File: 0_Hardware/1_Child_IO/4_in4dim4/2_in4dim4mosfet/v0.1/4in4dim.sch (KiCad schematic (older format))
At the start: 78 parts, among them IC1 TLP290, J1 RJ45, J2 RJ45, P1 CONN_5, P110 CONN_2, P120 CONN_2, P130 CONN_2, P140 CONN_2, P2 CONN_2, P3 CONN_8X2, Q1 SPP20N60C3, Q2 SPP20N60C3, Q3 SPP20N60C3, Q4 SPP20N60C3, U2 LTV847, U3 LTV847

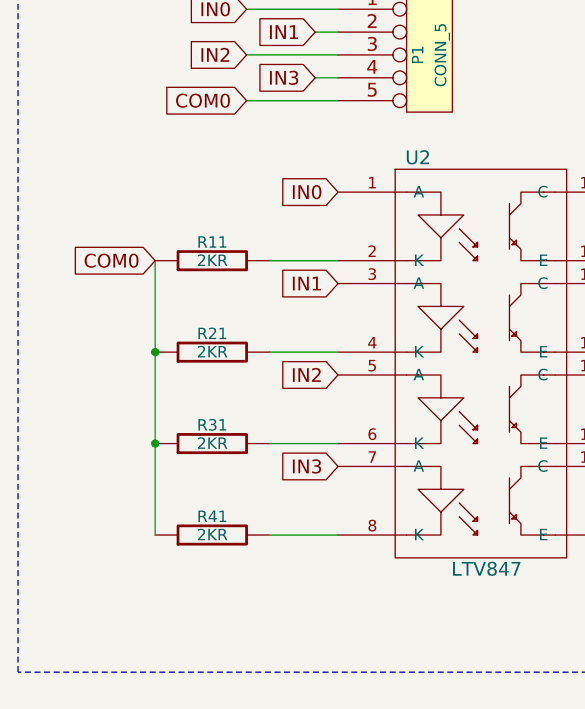
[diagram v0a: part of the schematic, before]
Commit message: mis à jour de la carte de puissance et de la front panel
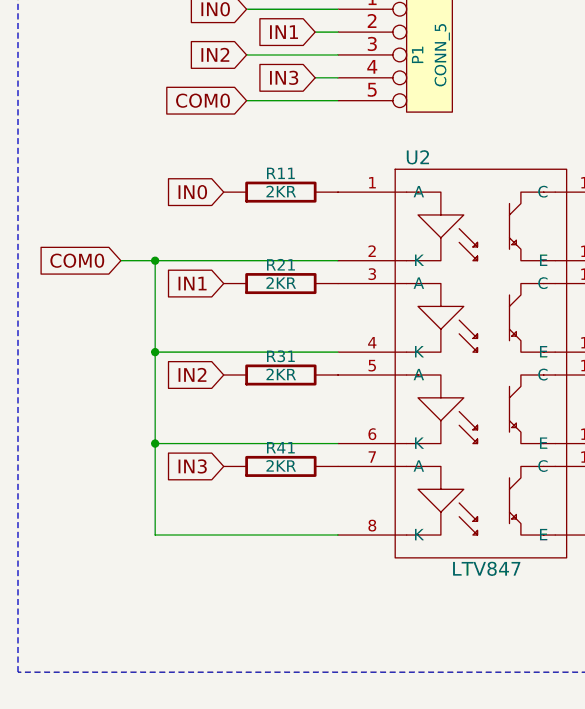
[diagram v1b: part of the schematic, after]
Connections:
- net COM0: now also U2.2 (K), U2.4 (K), U2.6 (K), U2.8 (K); no longer R11.1, R21.1, R31.1, R41.1
- net IN0: now also R11.1; no longer U2.1 (A)
- net IN1: now also R21.1; no longer U2.3 (A)
- net IN2: now also R31.1; no longer U2.5 (A)
- net IN3: now also R41.1; no longer U2.7 (A)
- net at R11.2: now also U2.1 (A); no longer U2.2 (K)
- net at R21.2: now also U2.3 (A); no longer U2.4 (K)
- net at R31.2: now also U2.5 (A); no longer U2.6 (K)
- net at R41.2: now also U2.7 (A); no longer U2.8 (K)
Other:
- moved on the sheet: R11, R21, R31, R41
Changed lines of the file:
@@
 LIBS:max485
 LIBS:4in4dim-cache
-EELAYER 24 0
+EELAYER 27 0
 EELAYER END
 $Descr A2 23386 16535
@@
 Sheet 1 1
 Title "4in 4dim power mosfet board"
-Date "10 mars 2014"
+Date "16 nov 2014"
 Rev "V0.0"
 Comp "XPLDUINO project"
@@
 L R R11
 U 1 1 51150759
-P 1900 2850
-F 0 "R11" V 1980 2850 50  0000 C CNN
-F 1 "2KR" V 1900 2850 50  0000 C CNN
-F 2 "" H 1900 2850 60  0001 C CNN
-F 3 "" H 1900 2850 60  0001 C CNN
-	1    1900 2850
+P 2200 2550
+F 0 "R11" V 2280 2550 50  0000 C CNN
+F 1 "2KR" V 2200 2550 50  0000 C CNN
+F 2 "" H 2200 2550 60  0001 C CNN
+F 3 "" H 2200 2550 60  0001 C CNN
+	1    2200 2550
 	0    -1   -1   0
 $EndComp
@@
 L R R21
 U 1 1 51150EEF
-P 1900 3250
-F 0 "R21" V 1980 3250 50  0000 C CNN
-F 1 "2KR" V 1900 3250 50  0000 C CNN
-F 2 "" H 1900 3250 60  0001 C CNN
-F 3 "" H 1900 3250 60  0001 C CNN
-	1    1900 3250
+P 2200 2950
+F 0 "R21" V 2280 2950 50  0000 C CNN
+F 1 "2KR" V 2200 2950 50  0000 C CNN
+F 2 "" H 2200 2950 60  0001 C CNN
+F 3 "" H 2200 2950 60  0001 C CNN
+	1    2200 2950
 	0    -1   -1   0
 $EndComp
@@
 L R R31
 U 1 1 51151110
-P 1900 3650
-F 0 "R31" V 1980 3650 50  0000 C CNN
-F 1 "2KR" V 1900 3650 50  0000 C CNN
-F 2 "" H 1900 3650 60  0001 C CNN
-F 3 "" H 1900 3650 60  0001 C CNN
-	1    1900 3650
+P 2200 3350
+F 0 "R31" V 2280 3350 50  0000 C CNN
+F 1 "2KR" V 2200 3350 50  0000 C CNN
+F 2 "" H 2200 3350 60  0001 C CNN
+F 3 "" H 2200 3350 60  0001 C CNN
+	1    2200 3350
 	0    -1   -1   0
 $EndComp
@@
 L R R41
 U 1 1 51151157
-P 1900 4050
-F 0 "R41" V 1980 4050 50  0000 C CNN
-F 1 "2KR" V 1900 4050 50  0000 C CNN
-F 2 "" H 1900 4050 60  0001 C CNN
-F 3 "" H 1900 4050 60  0001 C CNN
-	1    1900 4050
+P 2200 3750
+F 0 "R41" V 2280 3750 50  0000 C CNN
+F 1 "2KR" V 2200 3750 50  0000 C CNN
+F 2 "" H 2200 3750 60  0001 C CNN
+F 3 "" H 2200 3750 60  0001 C CNN
+	1    2200 3750
 	0    -1   -1   0
 $EndComp
@@
 Text GLabel 7450 7150 3    60   Input ~ 0
 /INT
-Text GLabel 2450 2550 0    60   Input ~ 0
+Text GLabel 1950 2550 0    60   Input ~ 0
 IN0
-Text GLabel 2450 2950 0    60   Input ~ 0
+Text GLabel 1950 2950 0    60   Input ~ 0
 IN1
-Text GLabel 2450 3350 0    60   Input ~ 0
+Text GLabel 1950 3350 0    60   Input ~ 0
 IN2
-Text GLabel 2450 3750 0    60   Input ~ 0
+Text GLabel 1950 3750 0    60   Input ~ 0
 IN3
 Text GLabel 8500 13700 2    60   BiDi ~ 0
@@
 Text GLabel 8200 13800 2    60   BiDi ~ 0
 SCL
-Text GLabel 1650 2850 0    60   Input ~ 0
+Text GLabel 1500 2850 0    60   Input ~ 0
 COM0
 $Comp
@@
 	9650 12600 5350 12600
 Wire Wire Line
-	2150 4050 2450 4050
-Wire Wire Line
-	2150 3650 2450 3650
-Wire Wire Line
-	2150 3250 2450 3250
-Wire Wire Line
-	2150 2850 2450 2850
+	1650 4050 2450 4050
+Wire Wire Line
+	1650 3650 2450 3650
+Wire Wire Line
+	1650 3250 2450 3250
+Wire Wire Line
+	1500 2850 2450 2850
 Wire Wire Line
 	1650 2850 1650 4050
@@
 	8050 13600 8250 13600
 NoConn ~ 7250 13600
+Connection ~ 1650 2850
 $EndSCHEMATC

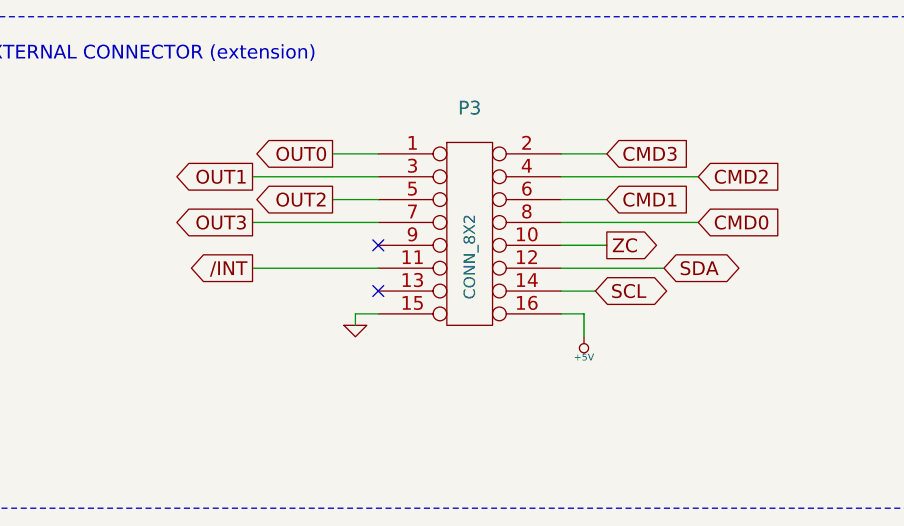
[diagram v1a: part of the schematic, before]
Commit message: Carte de puissance dimmer - modification du connecteur 20 broches: doublement de 5V et GND et optimisation pinout - modification empreinte des optos 4 canaux et single (création boitier DDIP16 et DDIP4) suite controle des packages des composants - routage pour tenir compte des changements de packages
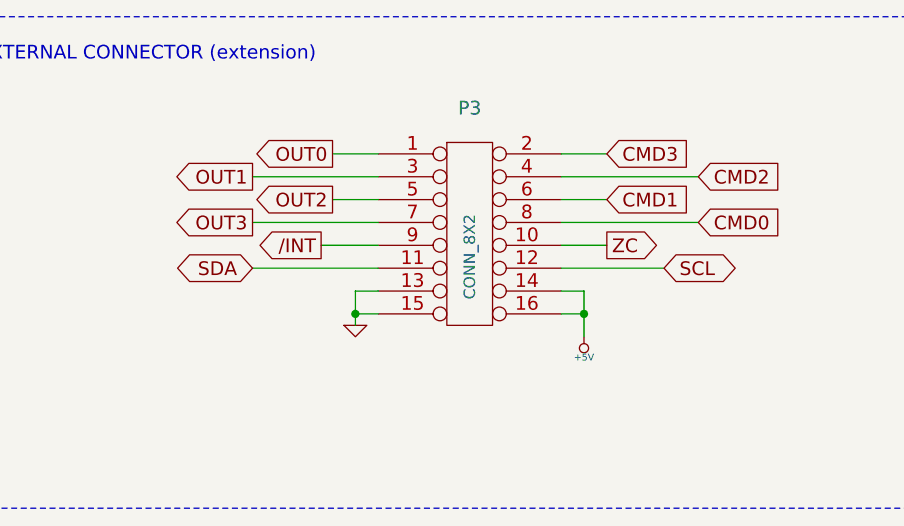
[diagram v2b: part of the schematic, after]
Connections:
- net +5V: now also P3.14
- net /INT: now also P3.9; no longer P3.11
- net GND: now also P3.13
- net SCL: now also P3.12; no longer P3.14
- net SDA: now also P3.11; no longer P3.12
- no-connect marks 2 -> 0
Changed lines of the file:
@@
 Sheet 1 1
 Title "4in 4dim power mosfet board"
-Date "16 nov 2014"
+Date "19 nov 2014"
 Rev "V0.0"
 Comp "XPLDUINO project"
@@
 Text GLabel 6150 7150 3    60   BiDi ~ 0
 SCL
-Text GLabel 6700 13700 0    60   Output ~ 0
+Text GLabel 7000 13600 0    60   Output ~ 0
 /INT
 Text GLabel 6350 7150 3    60   Input ~ 0
@@
 Text GLabel 1950 3750 0    60   Input ~ 0
 IN3
+Text GLabel 6700 13700 0    60   BiDi ~ 0
+SDA
 Text GLabel 8500 13700 2    60   BiDi ~ 0
-SDA
-Text GLabel 8200 13800 2    60   BiDi ~ 0
 SCL
 Text GLabel 1500 2850 0    60   Input ~ 0
@@
 	1    0    0    -1
 $EndComp
+Text Label 15350 5050 0    60   ~ 0
+110D
+Text Label 16550 7200 0    60   ~ 0
+110S
+Text Label 16650 12300 0    60   ~ 0
+120S
+Text Label 15400 10150 0    60   ~ 0
+120D
+Text Label 20200 5050 0    60   ~ 0
+130D
+Text Label 20250 10150 0    60   ~ 0
+140D
+Text Label 21400 7200 0    60   ~ 0
+130S
+Text Label 21450 12300 0    60   ~ 0
+140S
+$Comp
+L R RP1
+U 1 1 53162006
+P 18850 2000
+F 0 "RP1" V 18930 2000 50  0000 C CNN
+F 1 "0R" V 18850 2000 50  0000 C CNN
+F 2 "" H 18850 2000 60  0001 C CNN
+F 3 "" H 18850 2000 60  0001 C CNN
+	1    18850 2000
+	0    -1   -1   0
+$EndComp
+$Comp
+L R RP2
+U 1 1 53162029
+P 18850 2200
+F 0 "RP2" V 18930 2200 50  0000 C CNN
+F 1 "0R" V 18850 2200 50  0000 C CNN
+F 2 "" H 18850 2200 60  0001 C CNN
+F 3 "" H 18850 2200 60  0001 C CNN
+	1    18850 2200
+	0    -1   -1   0
+$EndComp
+$Comp
+L R RP3
+U 1 1 5316202F
+P 18850 2400
+F 0 "RP3" V 18930 2400 50  0000 C CNN
+F 1 "0R" V 18850 2400 50  0000 C CNN
+F 2 "" H 18850 2400 60  0001 C CNN
+F 3 "" H 18850 2400 60  0001 C CNN
+	1    18850 2400
+	0    -1   -1   0
+$EndComp
+$Comp
+L R RP4
+U 1 1 5316203F
+P 18850 2600
+F 0 "RP4" V 18930 2600 50  0000 C CNN
+F 1 "0R" V 18850 2600 50  0000 C CNN
+F 2 "" H 18850 2600 60  0001 C CNN
+F 3 "" H 18850 2600 60  0001 C CNN
+	1    18850 2600
+	0    -1   -1   0
+$EndComp
+$Comp
+L R RP5
+U 1 1 53162045
+P 18850 2800
+F 0 "RP5" V 18930 2800 50  0000 C CNN
+F 1 "0R" V 18850 2800 50  0000 C CNN
+F 2 "" H 18850 2800 60  0001 C CNN
+F 3 "" H 18850 2800 60  0001 C CNN
+	1    18850 2800
+	0    -1   -1   0
+$EndComp
+$Comp
+L R RP6
+U 1 1 5316204B
+P 18850 3000
+F 0 "RP6" V 18930 3000 50  0000 C CNN
+F 1 "0R" V 18850 3000 50  0000 C CNN
+F 2 "" H 18850 3000 60  0001 C CNN
+F 3 "" H 18850 3000 60  0001 C CNN
+	1    18850 3000
+	0    -1   -1   0
+$EndComp
+$Comp
+L R RP7
+U 1 1 53162051
+P 18850 3200
+F 0 "RP7" V 18930 3200 50  0000 C CNN
+F 1 "0R" V 18850 3200 50  0000 C CNN
+F 2 "" H 18850 3200 60  0001 C CNN
+F 3 "" H 18850 3200 60  0001 C CNN
+	1    18850 3200
+	0    -1   -1   0
+$EndComp
+$Comp
+L R RP8
+U 1 1 5316205C
+P 18850 3400
+F 0 "RP8" V 18930 3400 50  0000 C CNN
+F 1 "0R" V 18850 3400 50  0000 C CNN
+F 2 "" H 18850 3400 60  0001 C CNN
+F 3 "" H 18850 3400 60  0001 C CNN
+	1    18850 3400
+	0    -1   -1   0
+$EndComp
+Text GLabel 8250 13600 2    60   Output ~ 0
+ZC
+$Comp
+L CONN_8X2 P3
+U 1 1 5136E504
+P 7650 13550
+F 0 "P3" H 7650 14100 60  0000 C CNN
+F 1 "CONN_8X2" V 7650 13450 50  0000 C CNN
+F 2 "" H 7650 13550 60  0000 C CNN
+F 3 "" H 7650 13550 60  0000 C CNN
+	1    7650 13550
+	1    0    0    -1
+$EndComp
+$Comp
+L TLP290 IC1
+U 1 1 53553DBA
+P 7100 9750
+F 0 "IC1" H 6890 9940 40  0000 C CNN
+F 1 "TLP290" H 7250 9560 40  0000 C CNN
+F 2 "SOP4" H 6910 9570 30  0000 C CIN
+F 3 "" H 7100 9750 60  0000 C CNN
+	1    7100 9750
+	1    0    0    -1
+$EndComp
+$Comp
+L R R1
+U 1 1 53553DC7
+P 6550 8800
+F 0 "R1" H 6400 8700 50  0000 C CNN
+F 1 "56K 1W" H 6300 8900 50  0000 C CNN
+F 2 "" H 6550 8800 60  0001 C CNN
+F 3 "" H 6550 8800 60  0001 C CNN
+	1    6550 8800
+	1    0    0    -1
+$EndComp
+$Comp
+L R R2
+U 1 1 53553DD7
+P 6550 9300
+F 0 "R2" H 6400 9200 50  0000 C CNN
+F 1 "56K 1W" H 6300 9400 50  0000 C CNN
+F 2 "" H 6550 9300 60  0001 C CNN
+F 3 "" H 6550 9300 60  0001 C CNN
+	1    6550 9300
+	1    0    0    -1
+$EndComp
+Text GLabel 6550 10000 3    60   Input ~ 0
+L
+Text GLabel 6550 8550 1    60   Input ~ 0
+N
+$Comp
+L GND #PWR015
+U 1 1 53554A15
+P 7700 10000
+F 0 "#PWR015" H 7700 10000 30  0001 C CNN
+F 1 "GND" H 7700 9930 30  0001 C CNN
+F 2 "" H 7700 10000 60  0001 C CNN
+F 3 "" H 7700 10000 60  0001 C CNN
+	1    7700 10000
+	1    0    0    -1
+$EndComp
+Text GLabel 7700 9500 1    60   Output ~ 0
+ZC
 Wire Notes Line
 	5350 8100 9650 8100
@@
 	6700 13500 7250 13500
 Wire Wire Line
-	7150 13950 7150 13900
+	7150 13800 7150 13950
 Wire Wire Line
 	7150 13900 7250 13900
 Wire Wire Line
 	8050 13900 8150 13900
-Wire Wire Line
-	8150 13900 8150 14000
 Wire Wire Line
 	8650 13500 8050 13500
@@
 	13350 5900 13350 6050
 Connection ~ 13350 6050
-Text Label 15350 5050 0    60   ~ 0
-110D
-Text Label 16550 7200 0    60   ~ 0
-110S
-Text Label 16650 12300 0    60   ~ 0
-120S
-Text Label 15400 10150 0    60   ~ 0
-120D
-Text Label 20200 5050 0    60   ~ 0
-130D
-Text Label 20250 10150 0    60   ~ 0
-140D
-Text Label 21400 7200 0    60   ~ 0
-130S
-Text Label 21450 12300 0    60   ~ 0
-140S
-$Comp
-L R RP1
-U 1 1 53162006
-P 18850 2000
-F 0 "RP1" V 18930 2000 50  0000 C CNN
-F 1 "0R" V 18850 2000 50  0000 C CNN
-F 2 "" H 18850 2000 60  0001 C CNN
-F 3 "" H 18850 2000 60  0001 C CNN
-	1    18850 2000
-	0    -1   -1   0
-$EndComp
-$Comp
-L R RP2
-U 1 1 53162029
-P 18850 2200
-F 0 "RP2" V 18930 2200 50  0000 C CNN
-F 1 "0R" V 18850 2200 50  0000 C CNN
-F 2 "" H 18850 2200 60  0001 C CNN
-F 3 "" H 18850 2200 60  0001 C CNN
-	1    18850 2200
-	0    -1   -1   0
-$EndComp
-$Comp
-L R RP3
-U 1 1 5316202F
-P 18850 2400
-F 0 "RP3" V 18930 2400 50  0000 C CNN
-F 1 "0R" V 18850 2400 50  0000 C CNN
-F 2 "" H 18850 2400 60  0001 C CNN
-F 3 "" H 18850 2400 60  0001 C CNN
-	1    18850 2400
-	0    -1   -1   0
-$EndComp
-$Comp
-L R RP4
-U 1 1 5316203F
-P 18850 2600
-F 0 "RP4" V 18930 2600 50  0000 C CNN
-F 1 "0R" V 18850 2600 50  0000 C CNN
-F 2 "" H 18850 2600 60  0001 C CNN
-F 3 "" H 18850 2600 60  0001 C CNN
-	1    18850 2600
-	0    -1   -1   0
-$EndComp
-$Comp
-L R RP5
-U 1 1 53162045
-P 18850 2800
-F 0 "RP5" V 18930 2800 50  0000 C CNN
-F 1 "0R" V 18850 2800 50  0000 C CNN
-F 2 "" H 18850 2800 60  0001 C CNN
-F 3 "" H 18850 2800 60  0001 C CNN
-	1    18850 2800
-	0    -1   -1   0
-$EndComp
-$Comp
-L R RP6
-U 1 1 5316204B
-P 18850 3000
-F 0 "RP6" V 18930 3000 50  0000 C CNN
-F 1 "0R" V 18850 3000 50  0000 C CNN
-F 2 "" H 18850 3000 60  0001 C CNN
-F 3 "" H 18850 3000 60  0001 C CNN
-	1    18850 3000
-	0    -1   -1   0
-$EndComp
-$Comp
-L R RP7
-U 1 1 53162051
-P 18850 3200
-F 0 "RP7" V 18930 3200 50  0000 C CNN
-F 1 "0R" V 18850 3200 50  0000 C CNN
-F 2 "" H 18850 3200 60  0001 C CNN
-F 3 "" H 18850 3200 60  0001 C CNN
-	1    18850 3200
-	0    -1   -1   0
-$EndComp
-$Comp
-L R RP8
-U 1 1 5316205C
-P 18850 3400
-F 0 "RP8" V 18930 3400 50  0000 C CNN
-F 1 "0R" V 18850 3400 50  0000 C CNN
-F 2 "" H 18850 3400 60  0001 C CNN
-F 3 "" H 18850 3400 60  0001 C CNN
-	1    18850 3400
-	0    -1   -1   0
-$EndComp
 Wire Wire Line
 	16300 3250 17250 3250
@@
 Connection ~ 16300 1950
 Wire Wire Line
-	8050 13800 8200 13800
-Wire Wire Line
 	8050 13700 8500 13700
-Text GLabel 8250 13600 2    60   Output ~ 0
-ZC
+Wire Wire Line
+	6550 9550 6550 9650
+Wire Wire Line
+	6550 9650 6750 9650
+Wire Wire Line
+	6550 9850 6750 9850
+Wire Wire Line
+	6550 9850 6550 10000
+Wire Wire Line
+	7450 9650 7700 9650
+Wire Wire Line
+	7700 9650 7700 9500
+Wire Wire Line
+	7450 9850 7700 9850
+Wire Wire Line
+	7700 9850 7700 10000
+Wire Wire Line
+	8050 13600 8250 13600
+Connection ~ 1650 2850
+Wire Wire Line
+	7000 13600 7250 13600
 Wire Wire Line
 	6700 13700 7250 13700
-$Comp
-L CONN_8X2 P3
-U 1 1 5136E504
-P 7650 13550
-F 0 "P3" H 7650 14100 60  0000 C CNN
-F 1 "CONN_8X2" V 7650 13450 50  0000 C CNN
-F 2 "" H 7650 13550 60  0000 C CNN
-F 3 "" H 7650 13550 60  0000 C CNN
-	1    7650 13550
-	1    0    0    -1
-$EndComp
-NoConn ~ 7250 13800
-$Comp
-L TLP290 IC1
-U 1 1 53553DBA
-P 7100 9750
-F 0 "IC1" H 6890 9940 40  0000 C CNN
-F 1 "TLP290" H 7250 9560 40  0000 C CNN
-F 2 "SOP4" H 6910 9570 30  0000 C CIN
-F 3 "" H 7100 9750 60  0000 C CNN
-	1    7100 9750
-	1    0    0    -1
-$EndComp
-$Comp
-L R R1
-U 1 1 53553DC7
-P 6550 8800
-F 0 "R1" H 6400 8700 50  0000 C CNN
-F 1 "56K 1W" H 6300 8900 50  0000 C CNN
-F 2 "" H 6550 8800 60  0001 C CNN
-F 3 "" H 6550 8800 60  0001 C CNN
-	1    6550 8800
-	1    0    0    -1
-$EndComp
-$Comp
-L R R2
-U 1 1 53553DD7
-P 6550 9300
-F 0 "R2" H 6400 9200 50  0000 C CNN
-F 1 "56K 1W" H 6300 9400 50  0000 C CNN
-F 2 "" H 6550 9300 60  0001 C CNN
-F 3 "" H 6550 9300 60  0001 C CNN
-	1    6550 9300
-	1    0    0    -1
-$EndComp
-Wire Wire Line
-	6550 9550 6550 9650
-Wire Wire Line
-	6550 9650 6750 9650
-Wire Wire Line
-	6550 9850 6750 9850
-Wire Wire Line
-	6550 9850 6550 10000
-Text GLabel 6550 10000 3    60   Input ~ 0
-L
-Text GLabel 6550 8550 1    60   Input ~ 0
-N
-Wire Wire Line
-	7450 9650 7700 9650
-Wire Wire Line
-	7700 9650 7700 9500
-Wire Wire Line
-	7450 9850 7700 9850
-Wire Wire Line
-	7700 9850 7700 10000
-$Comp
-L GND #PWR015
-U 1 1 53554A15
-P 7700 10000
-F 0 "#PWR015" H 7700 10000 30  0001 C CNN
-F 1 "GND" H 7700 9930 30  0001 C CNN
-F 2 "" H 7700 10000 60  0001 C CNN
-F 3 "" H 7700 10000 60  0001 C CNN
-	1    7700 10000
-	1    0    0    -1
-$EndComp
-Text GLabel 7700 9500 1    60   Output ~ 0
-ZC
-Wire Wire Line
-	8050 13600 8250 13600
-NoConn ~ 7250 13600
-Connection ~ 1650 2850
+Wire Wire Line
+	7250 13800 7150 13800
+Connection ~ 7150 13900
+Connection ~ 8150 13900
+Wire Wire Line
+	8050 13800 8150 13800
+Wire Wire Line
+	8150 13800 8150 14000
 $EndSCHEMATC

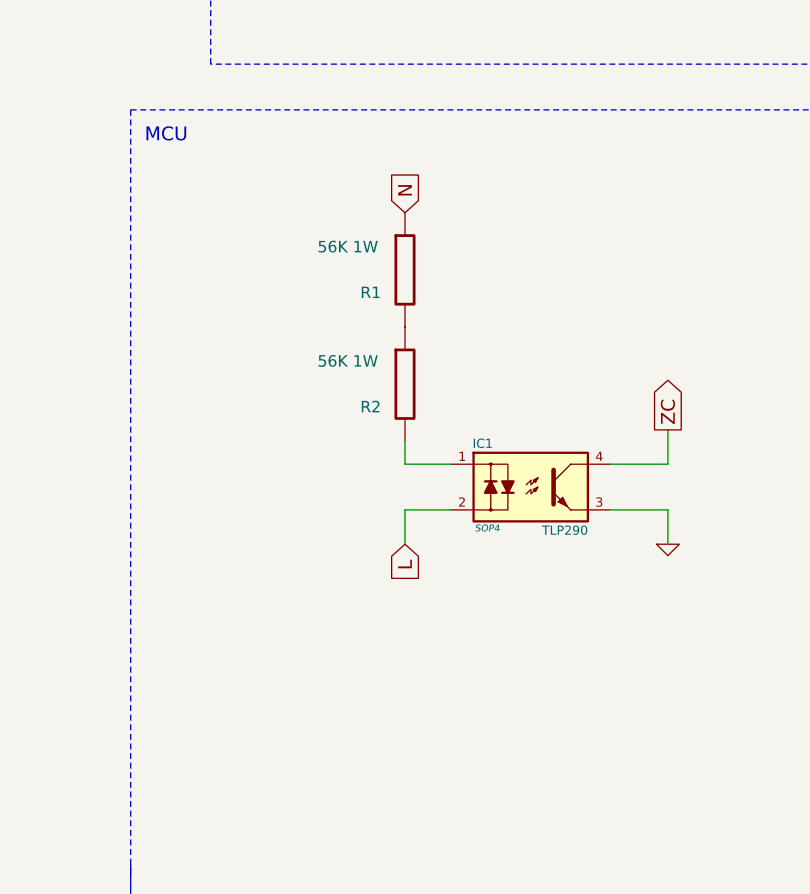
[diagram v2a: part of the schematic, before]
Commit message: IN4DIM4: remplacement empreinte PNP par SOT-23 standard
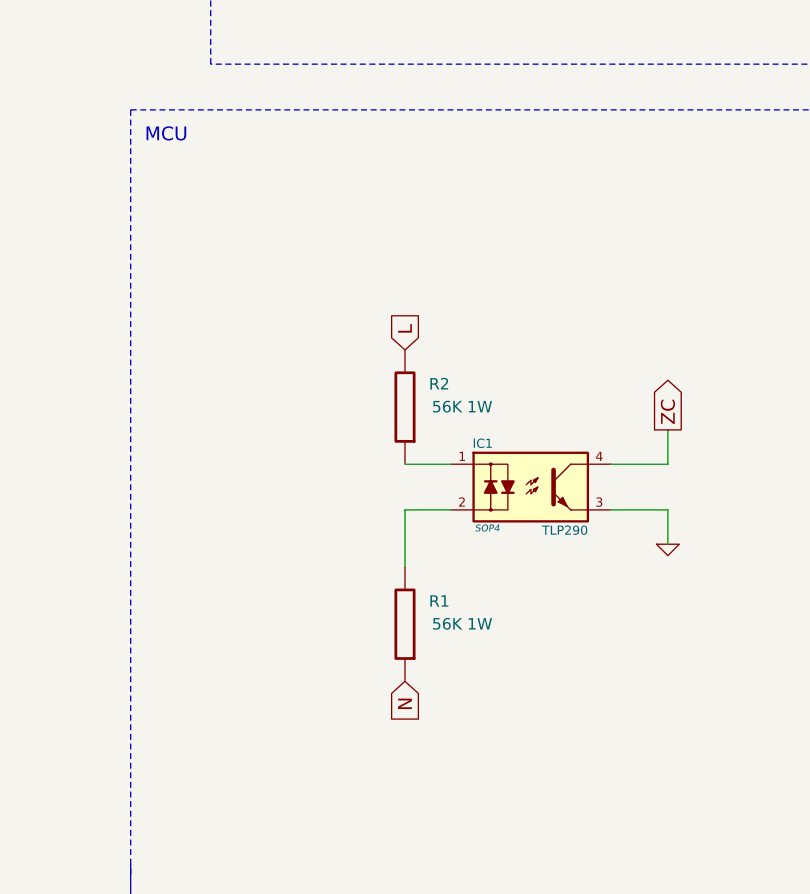
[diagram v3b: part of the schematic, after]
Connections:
- net L: now also R2.2; no longer IC1.2
- net at IC1.1: now also R2.1; no longer R2.2
- net at R1.2: now also IC1.2; no longer R2.1
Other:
- moved on the sheet: R1, R2
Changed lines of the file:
@@
 Sheet 1 1
 Title "4in 4dim power mosfet board"
-Date "19 nov 2014"
+Date "25 nov 2014"
 Rev "V0.0"
 Comp "XPLDUINO project"
@@
 L R R1
 U 1 1 53553DC7
-P 6550 8800
-F 0 "R1" H 6400 8700 50  0000 C CNN
-F 1 "56K 1W" H 6300 8900 50  0000 C CNN
-F 2 "" H 6550 8800 60  0001 C CNN
-F 3 "" H 6550 8800 60  0001 C CNN
-	1    6550 8800
-	1    0    0    -1
+P 6550 10350
+F 0 "R1" H 6400 10250 50  0000 C CNN
+F 1 "56K 1W" H 6300 10350 50  0000 C CNN
+F 2 "" H 6550 10350 60  0001 C CNN
+F 3 "" H 6550 10350 60  0001 C CNN
+	1    6550 10350
+	-1   0    0    1
 $EndComp
 $Comp
 L R R2
 U 1 1 53553DD7
-P 6550 9300
-F 0 "R2" H 6400 9200 50  0000 C CNN
+P 6550 9400
+F 0 "R2" H 6400 9300 50  0000 C CNN
 F 1 "56K 1W" H 6300 9400 50  0000 C CNN
-F 2 "" H 6550 9300 60  0001 C CNN
-F 3 "" H 6550 9300 60  0001 C CNN
-	1    6550 9300
-	1    0    0    -1
-$EndComp
-Text GLabel 6550 10000 3    60   Input ~ 0
+F 2 "" H 6550 9400 60  0001 C CNN
+F 3 "" H 6550 9400 60  0001 C CNN
+	1    6550 9400
+	-1   0    0    1
+$EndComp
+Text GLabel 6550 9150 1    60   Input ~ 0
 L
-Text GLabel 6550 8550 1    60   Input ~ 0
+Text GLabel 6550 10600 3    60   Input ~ 0
 N
 $Comp
@@
 	8050 13700 8500 13700
 Wire Wire Line
-	6550 9550 6550 9650
+	6550 9850 6550 10100
 Wire Wire Line
 	6550 9650 6750 9650
@@
 	6550 9850 6750 9850
 Wire Wire Line
-	6550 9850 6550 10000
-Wire Wire Line
 	7450 9650 7700 9650
